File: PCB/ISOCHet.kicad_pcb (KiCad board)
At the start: 2 copper layers, 57.1 x 38.1 mm, 19 parts, among them J1 USB_C_Receptacle_USB2.0, J2 Conn_01x08_Pin, SW0 BOOT, SW1 TAB, SW2 ENTER, SW3 CAPS, SW4 CAPS_STEP1.5, SW5 CAPS_STEP1.25, U1 CH552E, U2 USBLC6-2P6

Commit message: Prepare for production
 * Set fabrication flags.
 * Remove order number — cost is no different for a board this small.
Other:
- board text removed: "JLCJLCJLCJLC"
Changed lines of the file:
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@@
       (plot_on_all_layers_selection 0x0000000_00000000)
       (disableapertmacros false)
-      (usegerberextensions false)
-      (usegerberattributes true)
-      (usegerberadvancedattributes true)
-      (creategerberjobfile true)
+      (usegerberextensions true)
+      (usegerberattributes false)
+      (usegerberadvancedattributes false)
+      (creategerberjobfile false)
       (dashed_line_dash_ratio 12.000000)
       (dashed_line_gap_ratio 3.000000)
@@
       (psa4output false)
       (plotreference true)
-      (plotvalue true)
+      (plotvalue false)
       (plotinvisibletext false)
       (sketchpadsonfab false)
-      (subtractmaskfromsilk false)
+      (subtractmaskfromsilk true)
       (outputformat 1)
       (mirror false)
-      (drillshape 1)
+      (drillshape 0)
       (scaleselection 1)
-      (outputdirectory "")
+      (outputdirectory "./Gerbers")
     )
   )
@@
     (effects (font (size 0.7 0.7) (thickness 0.12) bold) (justify right mirror))
   )
-  (gr_text "JLCJLCJLCJLC" (at 174.65 69.05625) (layer "F.SilkS")
-    (effects (font (size 1 1) (thickness 0.15)))
-  )
   (gr_text "ISOCHět" (at 175.41875 63.344924) (layer "B.Mask")

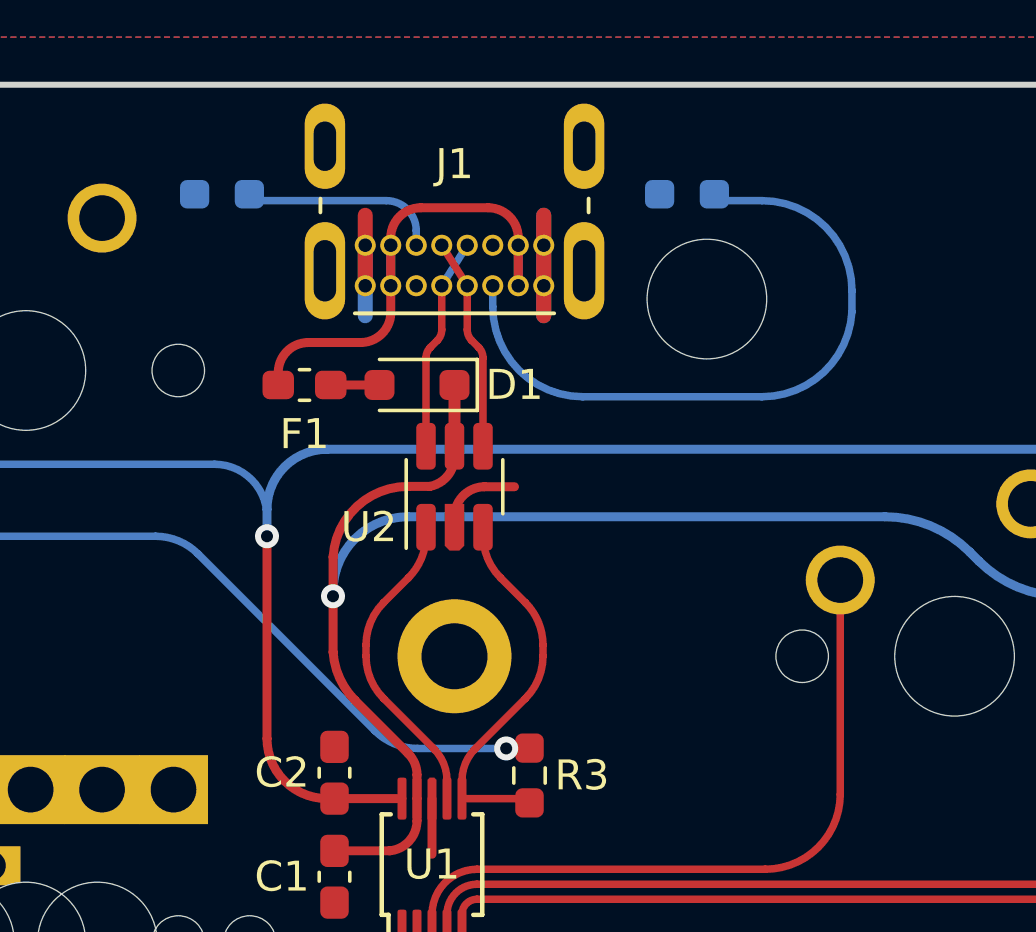
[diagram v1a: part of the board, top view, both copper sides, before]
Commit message: Isolate USD port ground from main PCB ground
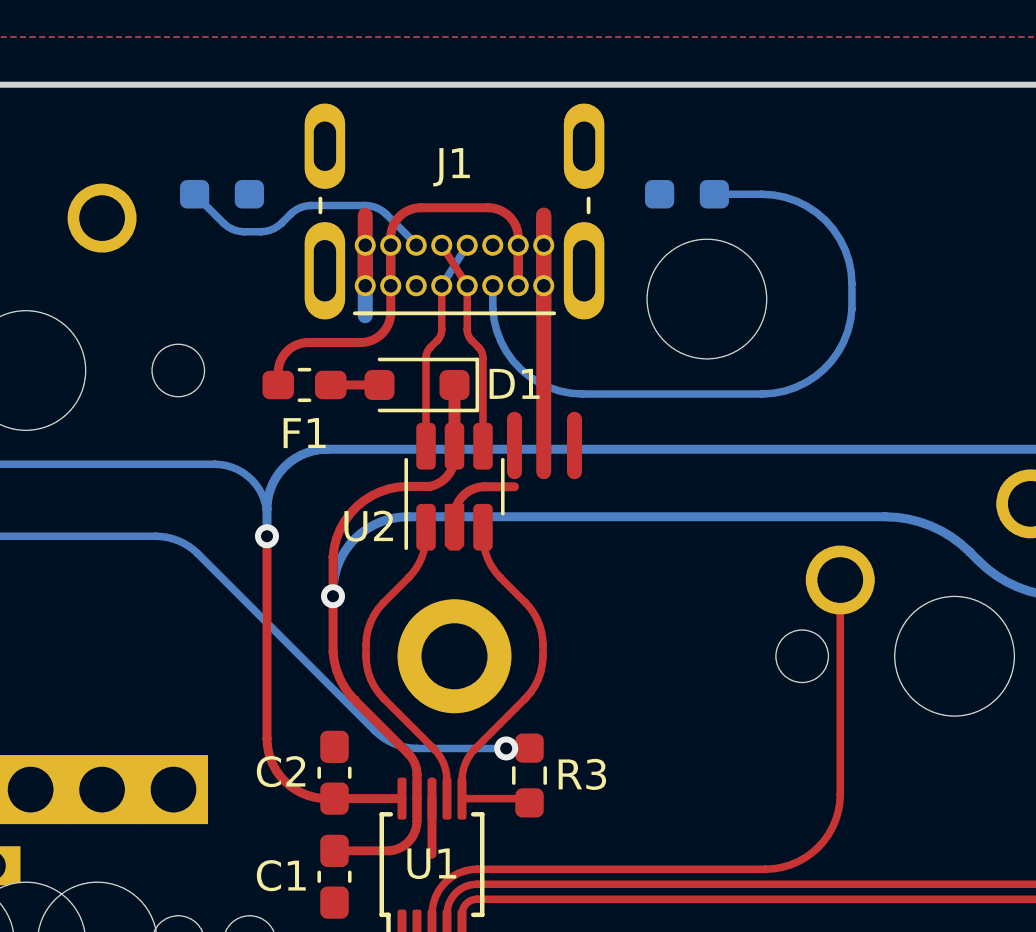
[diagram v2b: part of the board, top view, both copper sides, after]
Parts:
- turned R2 to 0 degrees
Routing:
- net GND: track 15.8 -> 24.5 mm
- net Net-(J1-CC2): track 6.58 -> 8.61 mm
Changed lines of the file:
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@@
   )
   (footprint "Resistor_SMD:R_0603_1608Metric_Pad0.98x0.95mm_HandSolder" (layer "B.Cu")
-    (at 151 41.75 180)
+    (at 151 41.75)
     (descr "Resistor SMD 0603 (1608 Metric), square (rectangular) end terminal, IPC_7351 nominal with elongated pad for handsoldering. (Body size source: IPC-SM-782 page 72, https://www.pcb-3d.com/wordpress/wp-content/uploads/ipc-sm-782a_amendment_1_and_2.pdf), generated with kicad-footprint-generator")
     (tags "resistor handsolder")
@@
     (property "ki_keywords" "R res resistor")
     (attr smd)
-    (fp_text reference "R2" (at 0 2.25) (layer "B.SilkS")
+    (fp_text reference "R2" (at 0 -2.25) (layer "B.SilkS")
         (effects (font (size 1 1) (thickness 0.15)) (justify mirror))
     )
@@
     (fp_line (start 0.8 0.4125) (end 0.8 -0.4125)
       (stroke (width 0.1) (type solid)) (layer "B.Fab"))
-    (pad "1" smd roundrect (at -0.9125 0 180) (size 0.975 0.95) (layers "B.Cu" "B.Paste" "B.Mask") (roundrect_rratio 0.25)
+    (pad "1" smd roundrect (at -0.9125 0) (size 0.975 0.95) (layers "B.Cu" "B.Paste" "B.Mask") (roundrect_rratio 0.25)
       (net 9 "Net-(J1-CC2)") (pintype "passive"))
-    (pad "2" smd roundrect (at 0.9125 0 180) (size 0.975 0.95) (layers "B.Cu" "B.Paste" "B.Mask") (roundrect_rratio 0.25)
+    (pad "2" smd roundrect (at 0.9125 0) (size 0.975 0.95) (layers "B.Cu" "B.Paste" "B.Mask") (roundrect_rratio 0.25)
       (net 2 "GND") (pintype "passive"))
     (model "${KICAD6_3DMODEL_DIR}/Resistor_SMD.3dshapes/R_0603_1608Metric.wrl"
@@
   (arc (start 157.2 52.5) (mid 155.432233 53.232233) (end 154.7 55) (width 0.3) (layer "B.Cu") (net 1))
   (arc (start 176.228427 53.978427) (mid 177.52612 54.845518) (end 179.056854 55.15) (width 0.3) (layer "B.Cu") (net 1))
-  (segment (start 161.725 42.45) (end 161.725 45.8) (width 0.5) (layer "F.Cu") (net 2))
+  (segment (start 161.725 42.45) (end 161.725 51) (width 0.5) (layer "F.Cu") (net 2))
   (segment (start 160.75 51.5) (end 159.75 51.5) (width 0.3) (layer "F.Cu") (net 2))
+  (segment (start 162.75 51) (end 162.75 49.25) (width 0.5) (layer "F.Cu") (net 2))
   (segment (start 158 63.75) (end 158 61.895) (width 0.3) (layer "F.Cu") (net 2))
   (segment (start 155.775 42.45) (end 155.775 44.8) (width 0.5) (layer "F.Cu") (net 2))
+  (segment (start 160.75 51) (end 160.75 49.25) (width 0.5) (layer "F.Cu") (net 2))
   (arc (start 159.75 51.5) (mid 159.042893 51.792893) (end 158.75 52.5) (width 0.3) (layer "F.Cu") (net 2))
-  (segment (start 155.775 43.45) (end 155.775 45.8) (width 0.5) (layer "B.Cu") (net 2))
   (segment (start 161.725 42.45) (end 161.725 45.8) (width 0.5) (layer "B.Cu") (net 2))
+  (segment (start 155.775 43.45) (end 155.775 45.8) (width 0.5) (layer "B.Cu") (net 2))
   (segment (start 154.625 48.1075) (end 156.25 48.1075) (width 0.3) (layer "F.Cu") (net 3))
   (segment (start 160.875 43.45) (end 160.875 43.2) (width 0.3) (layer "F.Cu") (net 4))
@@
   (segment (start 160.875 43.45) (end 160.875 44.8) (width 0.3) (layer "B.Cu") (net 4))
   (segment (start 156.625 43.45) (end 156.625 44.8) (width 0.3) (layer "B.Cu") (net 4))
-  (segment (start 171.997739 45.668349) (end 171.997739 44.964761) (width 0.25) (layer "B.Cu") (net 5))
-  (segment (start 171.997739 44.964761) (end 172 44.9625) (width 0.25) (layer "B.Cu") (net 5))
-  (segment (start 160.025 45.5) (end 160.025 44.8) (width 0.25) (layer "B.Cu") (net 5))
-  (segment (start 169 41.9625) (end 167.4125 41.9625) (width 0.25) (layer "B.Cu") (net 5))
-  (segment (start 163.025 48.5) (end 169 48.5) (width 0.25) (layer "B.Cu") (net 5))
-  (arc (start 172 44.9625) (mid 171.12132 42.84118) (end 169 41.9625) (width 0.25) (layer "B.Cu") (net 5))
-  (arc (start 160.025 45.5) (mid 160.90368 47.62132) (end 163.025 48.5) (width 0.25) (layer "B.Cu") (net 5))
-  (arc (start 169 48.5) (mid 171.060991 47.679981) (end 171.997739 45.668349) (width 0.25) (layer "B.Cu") (net 5))
+  (segment (start 169 48.408445) (end 163.025 48.408445) (width 0.25) (layer "B.Cu") (net 5))
+  (segment (start 167.4125 41.75) (end 169 41.75) (width 0.25) (layer "B.Cu") (net 5))
+  (segment (start 172 44.75) (end 171.997739 44.752261) (width 0.25) (layer "B.Cu") (net 5))
+  (segment (start 171.997739 44.873206) (end 171.997739 45.576794) (width 0.25) (layer "B.Cu") (net 5))
+  (segment (start 160.027261 45.576794) (end 160.027261 44.923206) (width 0.25) (layer "B.Cu") (net 5))
+  (arc (start 169 41.75) (mid 171.12132 42.62868) (end 172 44.75) (width 0.25) (layer "B.Cu") (net 5))
+  (arc (start 171.997739 45.576794) (mid 171.060991 47.588426) (end 169 48.408445) (width 0.25) (layer "B.Cu") (net 5))
+  (arc (start 163.025 48.408445) (mid 160.964009 47.588426) (end 160.027261 45.576794) (width 0.25) (layer "B.Cu") (net 5))
   (segment (start 159.7 47.207107) (end 159.7 50.15) (width 0.25) (layer "F.Cu") (net 6))
   (segment (start 159.321447 46.621447) (end 159.553554 46.853554) (width 0.25) (layer "F.Cu") (net 6))
@@
   (arc (start 157.8 47.207107) (mid 157.83806 47.015766) (end 157.946446 46.853554) (width 0.25) (layer "F.Cu") (net 7))
   (segment (start 158.325 44.8) (end 159.175 43.45) (width 0.25) (layer "B.Cu") (net 7))
-  (segment (start 157.475 42.9625) (end 157.475 43.45) (width 0.25) (layer "B.Cu") (net 9))
-  (segment (start 156.475 41.9625) (end 151.9125 41.9625) (width 0.25) (layer "B.Cu") (net 9))
-  (arc (start 157.475 42.9625) (mid 157.182107 42.255393) (end 156.475 41.9625) (width 0.25) (layer "B.Cu") (net 9))
+  (segment (start 152.992893 42.707107) (end 153.282108 42.417892) (width 0.25) (layer "B.Cu") (net 9))
+  (segment (start 150.0875 41.75) (end 151.044607 42.707107) (width 0.25) (layer "B.Cu") (net 9))
+  (segment (start 153.989215 42.124999) (end 155.769669 42.124999) (width 0.25) (layer "B.Cu") (net 9))
+  (segment (start 156.476776 42.417892) (end 157.475 43.416116) (width 0.25) (layer "B.Cu") (net 9))
+  (segment (start 151.751714 43) (end 152.285786 43) (width 0.25) (layer "B.Cu") (net 9))
+  (arc (start 151.044607 42.707107) (mid 151.36903 42.92388) (end 151.751714 43) (width 0.25) (layer "B.Cu") (net 9))
+  (arc (start 155.769669 42.124999) (mid 156.152352 42.201119) (end 156.476776 42.417892) (width 0.25) (layer "B.Cu") (net 9))
+  (arc (start 152.992893 42.707107) (mid 152.66847 42.92388) (end 152.285786 43) (width 0.25) (layer "B.Cu") (net 9))
+  (arc (start 153.282108 42.417892) (mid 153.606531 42.201119) (end 153.989215 42.124999) (width 0.25) (layer "B.Cu") (net 9))
   (segment (start 161.114213 55.364213) (end 160.285786 54.535786) (width 0.25) (layer "F.Cu") (net 11))
   (segment (start 161.7 57.143146) (end 161.7 56.778427) (width 0.25) (layer "F.Cu") (net 11))
@@
   (arc (start 161.7 56.778427) (mid 161.547759 56.01306) (end 161.114213 55.364213) (width 0.25) (layer "F.Cu") (net 11))
   (arc (start 161.114214 58.557359) (mid 161.547759 57.908513) (end 161.7 57.143146) (width 0.25) (layer "F.Cu") (net 11))
-  (segment (start 161.239414 60.223086) (end 161.25 60.2125) (width 0.25) (layer "F.Cu") (net 12))
   (segment (start 131.95 50.725) (end 131.95 44.525) (width 0.25) (layer "F.Cu") (net 12))
   (segment (start 137.5 53.15) (end 133.95 53.15) (width 0.25) (layer "F.Cu") (net 12))
@@
   (arc (start 179.25 64.75) (mid 180.664214 64.164214) (end 181.25 62.75) (width 0.25) (layer "F.Cu") (net 19))
   (arc (start 181.68934 59.155958) (mid 181.364181 59.642593) (end 181.25 60.216618) (width 0.25) (layer "F.Cu") (net 19))
+  (zone (net 0) (net_name "") (layer "F.Cu") (hatch none 0.5)
+    (connect_pads (clearance 0))
+    (min_thickness 0.25) (filled_areas_thickness no)
+    (keepout (tracks allowed) (vias allowed) (pads allowed) (copperpour not_allowed) (footprints allowed))
+    (fill (thermal_gap 0.5) (thermal_bridge_width 0.5))
+    (polygon
+      (pts
+        (xy 151.5 37.5)
+        (xy 151.5 49.875)
+        (xy 166 49.875)
+        (xy 166 37.5)
+        (xy 166.5 37.5)
+        (xy 166.5 50.125)
+        (xy 166.25 50.375)
+        (xy 151.25 50.375)
+        (xy 151 50.125)
+        (xy 151 37.5)
+      )
+    )
+  )
   (zone (net 2) (net_name "GND") (layers "F&B.Cu") (hatch edge 0.5)
     (connect_pads (clearance 0.5))
@@
       )
     )
+  )
+  (zone (net 0) (net_name "") (layer "B.Cu") (hatch none 0.5)
+    (connect_pads (clearance 0))
+    (min_thickness 0.25) (filled_areas_thickness no)
+    (keepout (tracks allowed) (vias allowed) (pads allowed) (copperpour not_allowed) (footprints allowed))
+    (fill (thermal_gap 0.5) (thermal_bridge_width 0.5))
+    (polygon
+      (pts
+        (xy 166.25 41.75)
+        (xy 166.25 37.75)
+        (xy 166.75 37.75)
+        (xy 166.75 41.75)
+      )
+    )
+  )
+  (zone (net 0) (net_name "") (layer "B.Cu") (hatch none 0.5)
+    (connect_pads (clearance 0))
+    (min_thickness 0.25) (filled_areas_thickness no)
+    (keepout (tracks allowed) (vias allowed) (pads allowed) (copperpour not_allowed) (footprints allowed))
+    (fill (thermal_gap 0.5) (thermal_bridge_width 0.5))
+    (polygon
+      (pts
+        (xy 151.5 42.5375)
+        (xy 151.5 48.5375)
+        (xy 162.75 48.5375)
+        (xy 162.75 49.0375)
+        (xy 151.25 49.0375)
+        (xy 151 48.7625)
+        (xy 151 42.5375)
+      )
+    )
+  )
+  (zone (net 0) (net_name "") (layer "B.Cu") (hatch none 0.5)
+    (connect_pads (clearance 0))
+    (min_thickness 0.25) (filled_areas_thickness no)
+    (keepout (tracks allowed) (vias allowed) (pads allowed) (copperpour not_allowed) (footprints allowed))
+    (fill (thermal_gap 0.5) (thermal_bridge_width 0.5))
+    (polygon
+      (pts
+        (xy 150.75 37.75)
+        (xy 150.75 41.75)
+        (xy 151.25 41.75)
+        (xy 151.25 37.75)
+      )
+    )

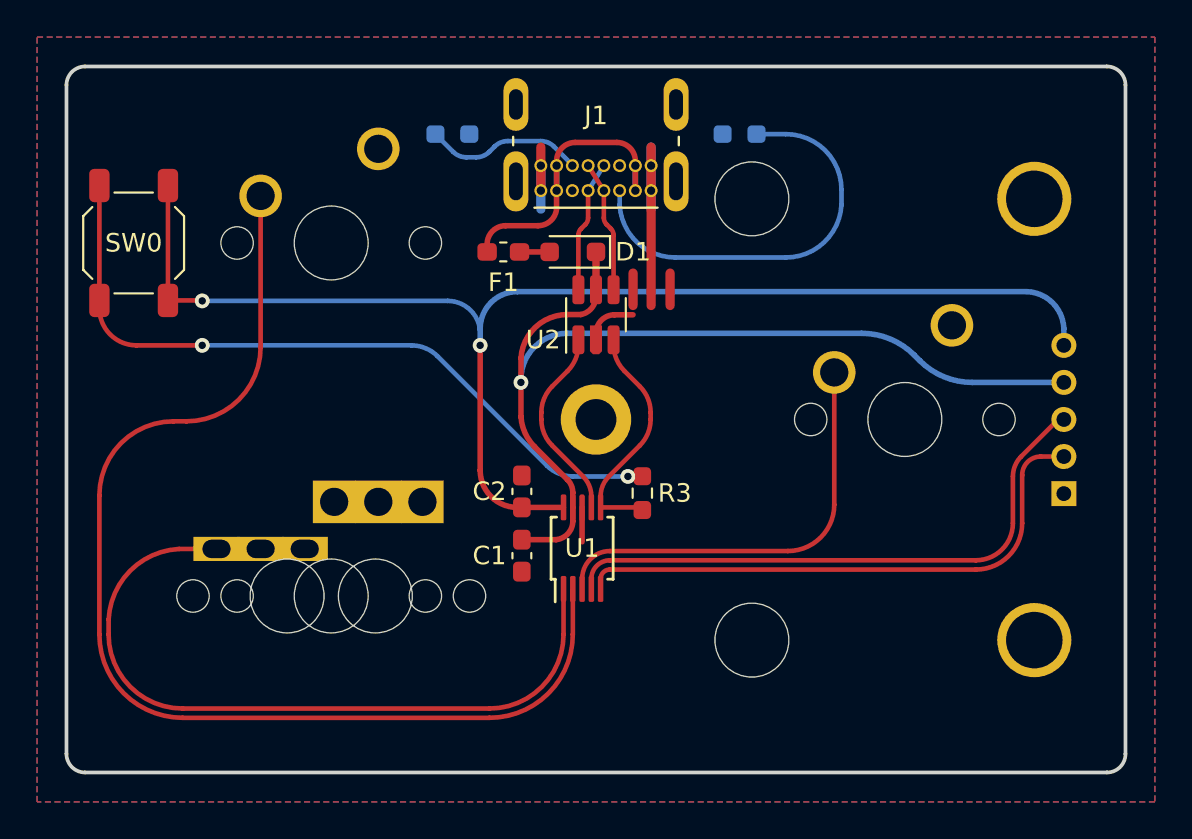
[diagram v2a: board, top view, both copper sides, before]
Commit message: Move CC1 such that it is before U1, not after
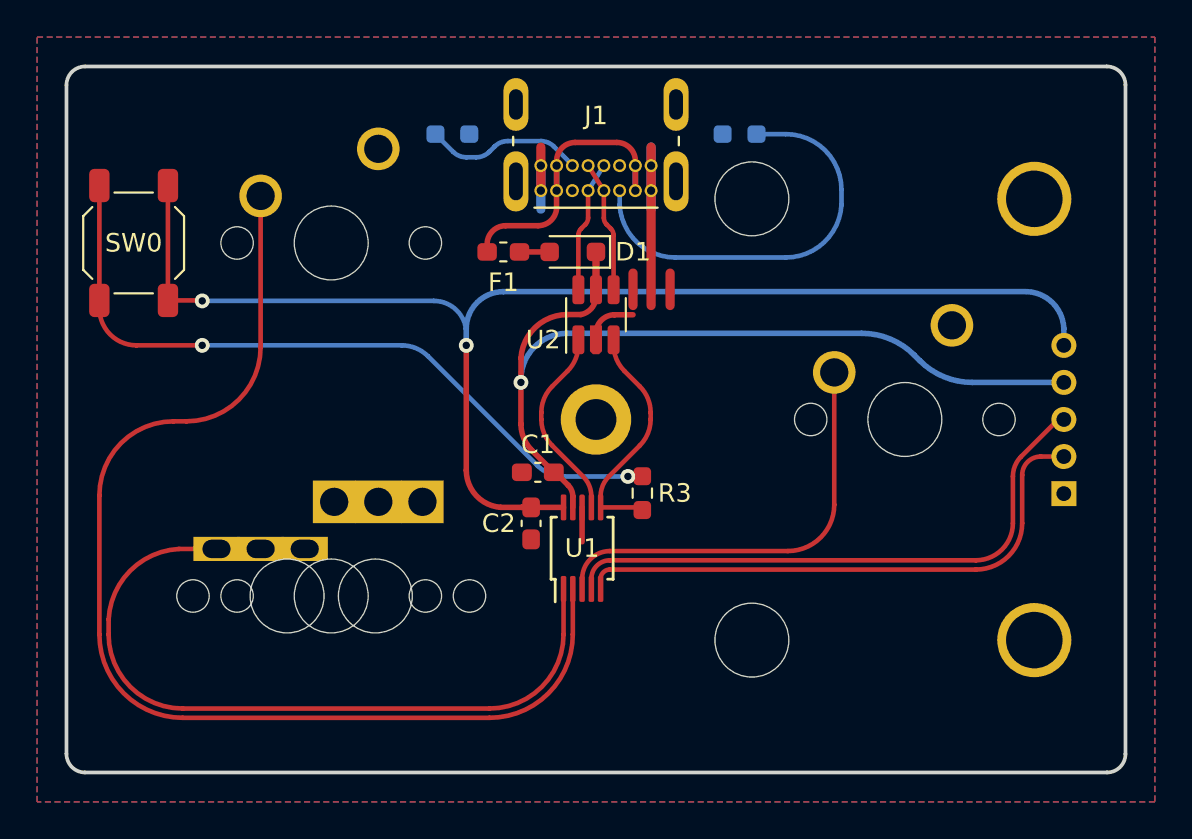
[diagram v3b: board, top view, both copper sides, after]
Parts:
- moved C1 4.58 mm to (155.6, 60.0), turned to 180 degrees
- moved C2 1.80 mm to (155.2, 62.8), turned to -90 degrees
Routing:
- net VCC: track 52.4 -> 48.4 mm
- net +3V3: track 72.1 -> 73.1 mm
